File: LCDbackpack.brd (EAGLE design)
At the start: 80 x 35.9 mm, 27 parts, among them IC1 74HC595N, IC2 LD117AV50, Q1 BS 170, U1 ATMEGA328P, U2 LCD-16X2NOHOLES, U3 LCD-16X2NOHOLES_NOSILK, Y1 16MHz

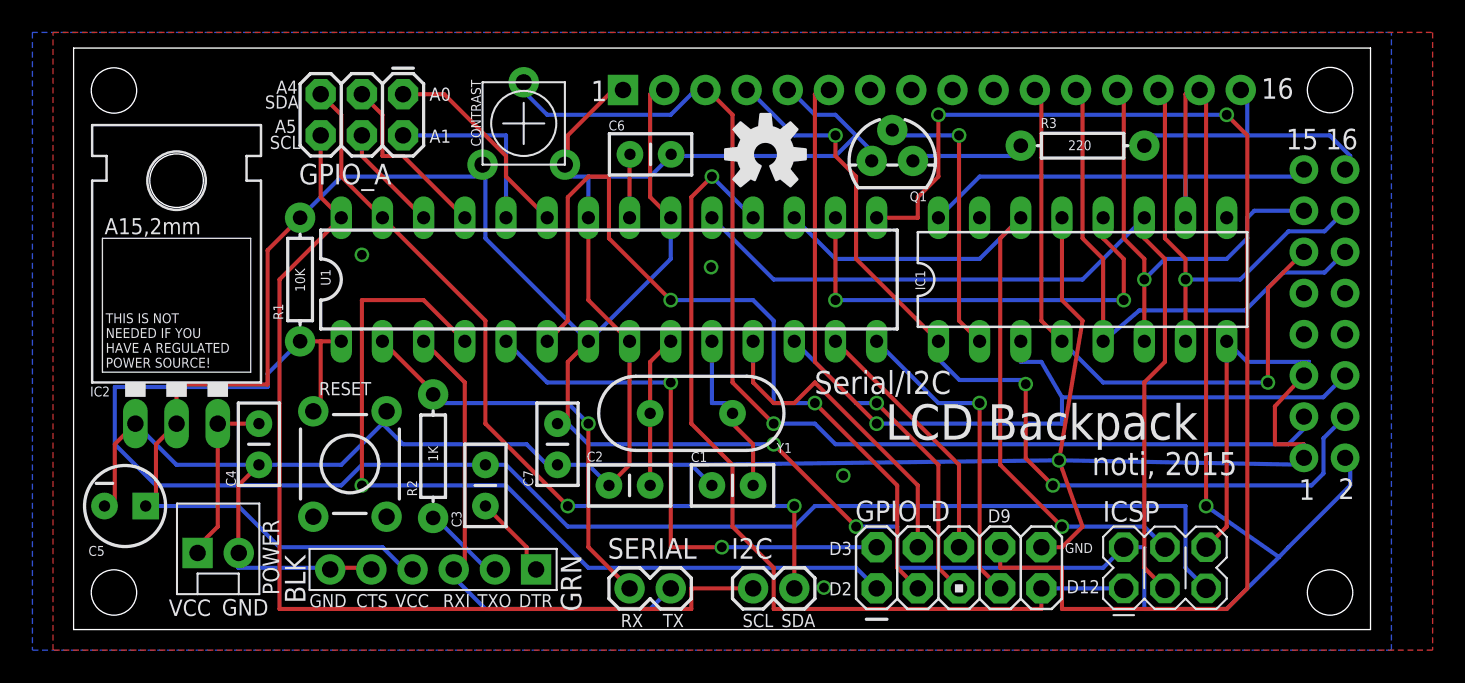
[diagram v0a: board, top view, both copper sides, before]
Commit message: Fixed isolation distance and created a library for the display
 - Fixed: the isolation distance on the ground fill was set to 0, which could cause a short
 - Added: Arduino library for driving the LCD
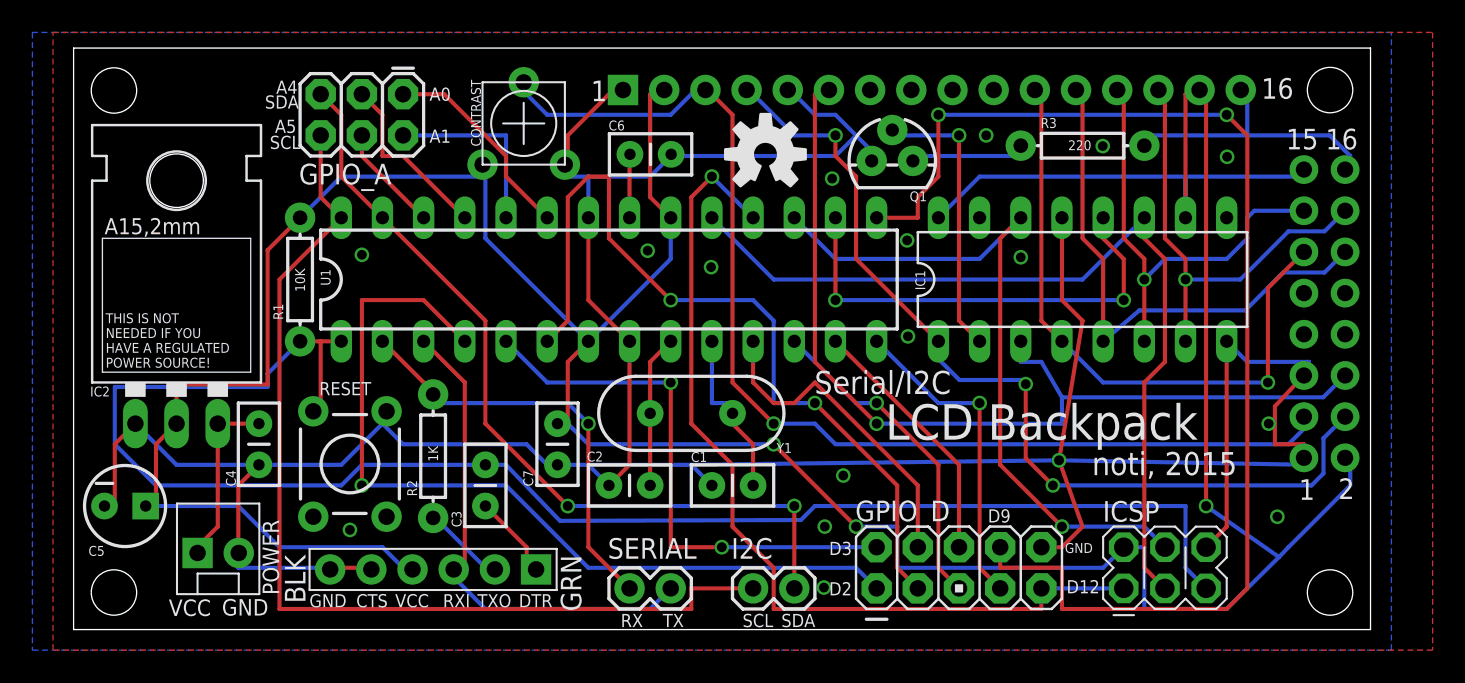
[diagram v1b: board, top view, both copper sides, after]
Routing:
- net GND: vias 5 -> 17
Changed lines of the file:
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@@
 <wire x1="29.21" y1="10.16" x2="29.845" y2="10.16" width="0.254" layer="16"/>
 <via x="60.7822" y="10.4394" extent="1-16" drill="0.6096"/>
-<polygon width="0.254" layer="16">
+<polygon width="0.254" layer="16" isolate="0.254">
 <vertex x="-2.54" y="36.83"/>
 <vertex x="-2.54" y="-1.27"/>
@@
 <vertex x="81.28" y="36.83"/>
 </polygon>
-<polygon width="0.254" layer="1">
+<polygon width="0.254" layer="1" isolate="0.254">
 <vertex x="83.82" y="36.83"/>
 <vertex x="83.82" y="-1.27"/>
@@
 <via x="47.4726" y="9.4996" extent="1-16" drill="0.6"/>
 <via x="46.2788" y="2.5908" extent="1-16" drill="0.6"/>
+<via x="46.7868" y="27.813" extent="1-16" drill="0.6"/>
+<via x="51.4096" y="24.003" extent="1-16" drill="0.6"/>
+<via x="51.4604" y="18.0848" extent="1-16" drill="0.6"/>
+<via x="56.2864" y="30.48" extent="1-16" drill="0.6"/>
+<via x="58.42" y="22.9616" extent="1-16" drill="0.6"/>
+<via x="35.4076" y="23.368" extent="1-16" drill="0.6"/>
+<via x="63.4746" y="29.8196" extent="1-16" drill="0.6"/>
+<via x="71.1454" y="29.1592" extent="1-16" drill="0.6"/>
+<via x="74.2442" y="6.9596" extent="1-16" drill="0.6"/>
+<via x="73.7108" y="12.7" extent="1-16" drill="0.6"/>
+<via x="17.0434" y="6.1468" extent="1-16" drill="0.6"/>
+<via x="46.3296" y="6.35" extent="1-16" drill="0.6"/>
 </signal>
 <signal name="VCC">
@@
 <wire x1="68.58" y1="7.62" x2="68.58" y2="3.81" width="0.254" layer="16"/>
 <wire x1="45.72" y1="7.62" x2="68.58" y2="7.62" width="0.254" layer="16"/>
-<wire x1="44.45" y1="6.35" x2="45.72" y2="7.62" width="0.254" layer="16"/>
-<wire x1="30.48" y1="6.35" x2="44.45" y2="6.35" width="0.254" layer="16"/>
-<wire x1="26.67" y1="10.16" x2="30.48" y2="6.35" width="0.254" layer="16"/>
+<wire x1="44.8564" y1="6.7564" x2="45.72" y2="7.62" width="0.254" layer="16"/>
+<wire x1="29.9974" y1="6.7056" x2="44.8564" y2="6.7564" width="0.254" layer="16"/>
+<wire x1="26.67" y1="10.16" x2="29.9974" y2="6.7056" width="0.254" layer="16"/>
 <wire x1="25.4" y1="10.16" x2="26.67" y2="10.16" width="0.254" layer="16"/>
 <wire x1="15.24" y1="17.78" x2="15.24" y2="13.97" width="0.254" layer="1"/>
